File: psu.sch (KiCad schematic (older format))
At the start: 72 parts, among them J10 1053091202, Q10 SQS401EN-T1_BE3, Q5 BSS84PH6327XTSA2, Q6 Si7223DN, Q8 Si7223DN, Q9 Si7223DN, U13 AP62301WU-7, U14 AP62301WU-7, U15 AP62301WU-7, U16 LMV431IM5, U17 AP62301WU-7, U21 LTC4417IUF

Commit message: Change USB-C connectors, continue layout
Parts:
- removed J10: 1053091202, sa800u-baseboard-hw-footprints:1053091202, symbol sa800u-baseboard-hw:1053091202
- added J10: 1053131202, antmicro-footprints:Molex_Nano-Fit_105313-xx02_1x02_P2.50mm_Horizontal, symbol antmicroRectangularConnectorsHeadersFemalePins:1053131202
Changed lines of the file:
@@
-$EndComp
-$Comp
-L sa800u-baseboard-hw:1053091202 J?
-U 1 1 61FFBF6D
-P 675 875
-AR Path="/61A19323/61FFBF6D" Ref="J?"  Part="1"
-AR Path="/61B0DC30/61FFBF6D" Ref="J10"  Part="1"
-F 0 "J10" H 783 1040 50  0000 C CNN
-F 1 "1053091202" H 783 949 50  0000 C CNN
-F 2 "sa800u-baseboard-hw-footprints:1053091202" H 500 550 50  0001 C CNN
-F 3 "" H 675 875 50  0001 C CNN
-F 4 "Molex" H 625 350 50  0001 C CNN "Manufacturer"
-F 5 "1053091202" H 550 425 50  0001 C CNN "MPN"
-	1    675  875
-	1    0    0    -1
 $EndComp
 $Comp
@@
 	0    1    1    0
 $EndComp
-Connection ~ 2500 6150
 $Comp
 L sa800u-baseboard-hw:R_13k7_0402 R140
@@
 	0    1    1    0
 $EndComp
-Connection ~ 2200 7200
-Connection ~ 2800 5100
 Wire Wire Line
 	7150 5000 7150 5250
@@
 Wire Wire Line
 	7150 4700 7150 4600
+$Comp
+L antmicroRectangularConnectorsHeadersFemalePins:1053131202 J10
+U 1 1 620EC9A9
+P 675 875
+F 0 "J10" H 783 1040 50  0000 C CNN
+F 1 "1053131202" H 783 949 50  0000 C CNN
+F 2 "antmicro-footprints:Molex_Nano-Fit_105313-xx02_1x02_P2.50mm_Horizontal" H 500 550 50  0001 C CNN
+F 3 "https://www.molex.com/molex/products/part-detail/pcb_headers/1053131202" H 675 875 50  0001 C CNN
+F 4 "Molex" H 625 350 50  0001 C CNN "Manufacturer"
+F 5 "1053131202" H 550 425 50  0001 C CNN "MPN"
+	1    675  875
+	1    0    0    -1
+$EndComp
 $EndSCHEMATC

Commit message: Change LED to KP-1608EC
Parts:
- J10: symbol antmicroRectangularConnectorsHeadersFemalePins:1053131202 -> sa800u-baseboard-hw-rescue:1053131202-antmicroRectangularConnectorsHeadersFemalePins
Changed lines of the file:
@@
 	7150 4700 7150 4600
 $Comp
-L antmicroRectangularConnectorsHeadersFemalePins:1053131202 J10
+L sa800u-baseboard-hw-rescue:1053131202-antmicroRectangularConnectorsHeadersFemalePins J10
 U 1 1 620EC9A9
 P 675 875
+AR Path="/620EC9A9" Ref="J10"  Part="1"
+AR Path="/61B0DC30/620EC9A9" Ref="J10"  Part="1"
 F 0 "J10" H 783 1040 50  0000 C CNN
 F 1 "1053131202" H 783 949 50  0000 C CNN

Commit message: Add test points
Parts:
- added D?: KP-1608EC, sa800u-baseboard-hw-footprints:LED_0603, symbol sa800u-baseboard-hw:KP-1608EC
- added R?: R_10k_0402, sa800u-baseboard-hw-footprints:0402-res, symbol sa800u-baseboard-hw:R_10k_0402
- added TP? (x24): TP_SMD_0_75MM, antmicro-footprints:Testpoint_smd_0_75mm, symbol antmicroTestPoints:TP_SMD_0_75MM
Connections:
- wire segments 237 -> 247

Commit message: Annotate test points, reimport 510R from global library
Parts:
- gave numbers to parts that had none: 26
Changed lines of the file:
@@
 	7125 1000 7125 950
 $Comp
-L sa800u-baseboard-hw:R_10k_0402 R?
+L sa800u-baseboard-hw:R_10k_0402 R57
 U 1 1 62114A3F
 P 7125 1150
-F 0 "R?" V 7170 1080 60  0000 R CNN
+F 0 "R57" V 7170 1080 60  0000 R CNN
 F 1 "R_10k_0402" H 7125 1000 60  0001 C CNN
 F 2 "sa800u-baseboard-hw-footprints:0402-res" H 7325 1350 60  0001 L CNN
@@
 $EndComp
 $Comp
-L sa800u-baseboard-hw:KP-1608EC D?
+L sa800u-baseboard-hw:KP-1608EC D30
 U 1 1 62114A47
 P 7125 1600
-F 0 "D?" V 6900 1625 60  0000 L CNN
+F 0 "D30" V 6900 1625 60  0000 L CNN
 F 1 "KP-1608EC" H 7075 1831 60  0001 C CNN
 F 2 "sa800u-baseboard-hw-footprints:LED_0603" H 7325 1800 60  0001 L CNN
@@
 P 7125 1700
 AR Path="/6215F5FF" Ref="#PWR?"  Part="1"
-AR Path="/61B0DC30/6215F5FF" Ref="#PWR?"  Part="1"
-F 0 "#PWR?" H 7125 1450 50  0001 C CNN
+AR Path="/61B0DC30/6215F5FF" Ref="#PWR0247"  Part="1"
+F 0 "#PWR0247" H 7125 1450 50  0001 C CNN
 F 1 "GND" H 7130 1527 50  0000 C CNN
 F 2 "" H 7125 1700 50  0001 C CNN
@@
 $EndComp
 $Comp
-L antmicroTestPoints:TP_SMD_0_75MM TP?
+L antmicroTestPoints:TP_SMD_0_75MM TP56
 U 1 1 621521C7
 P 12000 5950
-F 0 "TP?" H 11950 5997 50  0000 R CNN
+F 0 "TP56" H 11950 5997 50  0000 R CNN
 F 1 "TP_SMD_0_75MM" H 12000 5850 50  0001 C CNN
 F 2 "antmicro-footprints:Testpoint_smd_0_75mm" H 12200 6150 60  0001 L CNN
@@
 $EndComp
 $Comp
-L antmicroTestPoints:TP_SMD_0_75MM TP?
+L antmicroTestPoints:TP_SMD_0_75MM TP57
 U 1 1 62156A24
 P 12000 7325
-F 0 "TP?" H 11950 7372 50  0000 R CNN
+F 0 "TP57" H 11950 7372 50  0000 R CNN
 F 1 "TP_SMD_0_75MM" H 12000 7225 50  0001 C CNN
 F 2 "antmicro-footprints:Testpoint_smd_0_75mm" H 12200 7525 60  0001 L CNN
@@
 $EndComp
 $Comp
-L antmicroTestPoints:TP_SMD_0_75MM TP?
+L antmicroTestPoints:TP_SMD_0_75MM TP58
 U 1 1 621677D1
 P 12000 8700
-F 0 "TP?" H 11950 8747 50  0000 R CNN
+F 0 "TP58" H 11950 8747 50  0000 R CNN
 F 1 "TP_SMD_0_75MM" H 12000 8600 50  0001 C CNN
 F 2 "antmicro-footprints:Testpoint_smd_0_75mm" H 12200 8900 60  0001 L CNN
@@
 $EndComp
 $Comp
-L antmicroTestPoints:TP_SMD_0_75MM TP?
+L antmicroTestPoints:TP_SMD_0_75MM TP68
 U 1 1 6217A18F
 P 14625 8700
-F 0 "TP?" H 14575 8747 50  0000 R CNN
+F 0 "TP68" H 14575 8747 50  0000 R CNN
 F 1 "TP_SMD_0_75MM" H 14625 8600 50  0001 C CNN
 F 2 "antmicro-footprints:Testpoint_smd_0_75mm" H 14825 8900 60  0001 L CNN
@@
 $EndComp
 $Comp
-L antmicroTestPoints:TP_SMD_0_75MM TP?
+L antmicroTestPoints:TP_SMD_0_75MM TP67
 U 1 1 6218BBE3
 P 14625 7325
-F 0 "TP?" H 14575 7372 50  0000 R CNN
+F 0 "TP67" H 14575 7372 50  0000 R CNN
 F 1 "TP_SMD_0_75MM" H 14625 7225 50  0001 C CNN
 F 2 "antmicro-footprints:Testpoint_smd_0_75mm" H 14825 7525 60  0001 L CNN
@@
 $EndComp
 $Comp
-L antmicroTestPoints:TP_SMD_0_75MM TP?
+L antmicroTestPoints:TP_SMD_0_75MM TP66
 U 1 1 6219BCD7
 P 14625 5950
-F 0 "TP?" H 14575 5997 50  0000 R CNN
+F 0 "TP66" H 14575 5997 50  0000 R CNN
 F 1 "TP_SMD_0_75MM" H 14625 5850 50  0001 C CNN
 F 2 "antmicro-footprints:Testpoint_smd_0_75mm" H 14825 6150 60  0001 L CNN
@@
 $EndComp
 $Comp
-L antmicroTestPoints:TP_SMD_0_75MM TP?
+L antmicroTestPoints:TP_SMD_0_75MM TP61
 U 1 1 621AD212
 P 12325 6450
-F 0 "TP?" H 12375 6497 50  0000 L CNN
+F 0 "TP61" H 12375 6497 50  0000 L CNN
 F 1 "TP_SMD_0_75MM" H 12325 6350 50  0001 C CNN
 F 2 "antmicro-footprints:Testpoint_smd_0_75mm" H 12525 6650 60  0001 L CNN
@@
 $EndComp
 $Comp
-L antmicroTestPoints:TP_SMD_0_75MM TP?
+L antmicroTestPoints:TP_SMD_0_75MM TP62
 U 1 1 621BF886
 P 12325 7825
-F 0 "TP?" H 12375 7872 50  0000 L CNN
+F 0 "TP62" H 12375 7872 50  0000 L CNN
 F 1 "TP_SMD_0_75MM" H 12325 7725 50  0001 C CNN
 F 2 "antmicro-footprints:Testpoint_smd_0_75mm" H 12525 8025 60  0001 L CNN
@@
 $EndComp
 $Comp
-L antmicroTestPoints:TP_SMD_0_75MM TP?
+L antmicroTestPoints:TP_SMD_0_75MM TP63
 U 1 1 621D2B64
 P 12325 9200
-F 0 "TP?" H 12375 9247 50  0000 L CNN
+F 0 "TP63" H 12375 9247 50  0000 L CNN
 F 1 "TP_SMD_0_75MM" H 12325 9100 50  0001 C CNN
 F 2 "antmicro-footprints:Testpoint_smd_0_75mm" H 12525 9400 60  0001 L CNN
@@
 $EndComp
 $Comp
-L antmicroTestPoints:TP_SMD_0_75MM TP?
+L antmicroTestPoints:TP_SMD_0_75MM TP48
 U 1 1 621EF4D3
 P 5675 4800
-F 0 "TP?" H 5725 4847 50  0000 L CNN
+F 0 "TP48" H 5725 4847 50  0000 L CNN
 F 1 "TP_SMD_0_75MM" H 5675 4700 50  0001 C CNN
 F 2 "antmicro-footprints:Testpoint_smd_0_75mm" H 5875 5000 60  0001 L CNN
@@
 $EndComp
 $Comp
-L antmicroTestPoints:TP_SMD_0_75MM TP?
+L antmicroTestPoints:TP_SMD_0_75MM TP49
 U 1 1 62200067
 P 5975 4800
-F 0 "TP?" H 6025 4847 50  0000 L CNN
+F 0 "TP49" H 6025 4847 50  0000 L CNN
 F 1 "TP_SMD_0_75MM" H 5975 4700 50  0001 C CNN
 F 2 "antmicro-footprints:Testpoint_smd_0_75mm" H 6175 5000 60  0001 L CNN
@@
 $EndComp
 $Comp
-L antmicroTestPoints:TP_SMD_0_75MM TP?
+L antmicroTestPoints:TP_SMD_0_75MM TP51
 U 1 1 6220FE09
 P 6275 4800
-F 0 "TP?" H 6325 4847 50  0000 L CNN
+F 0 "TP51" H 6325 4847 50  0000 L CNN
 F 1 "TP_SMD_0_75MM" H 6275 4700 50  0001 C CNN
 F 2 "antmicro-footprints:Testpoint_smd_0_75mm" H 6475 5000 60  0001 L CNN
@@
 	6275 5250 7150 5250
 $Comp
-L antmicroTestPoints:TP_SMD_0_75MM TP?
+L antmicroTestPoints:TP_SMD_0_75MM TP47
 U 1 1 622544F5
 P 2800 850
-F 0 "TP?" H 2850 897 50  0000 L CNN
+F 0 "TP47" H 2850 897 50  0000 L CNN
 F 1 "TP_SMD_0_75MM" H 2800 750 50  0001 C CNN
 F 2 "antmicro-footprints:Testpoint_smd_0_75mm" H 3000 1050 60  0001 L CNN
@@
 $EndComp
 $Comp
-L antmicroTestPoints:TP_SMD_0_75MM TP?
+L antmicroTestPoints:TP_SMD_0_75MM TP46
 U 1 1 622544FB
 P 2500 1650
-F 0 "TP?" H 2550 1697 50  0000 L CNN
+F 0 "TP46" H 2550 1697 50  0000 L CNN
 F 1 "TP_SMD_0_75MM" H 2500 1550 50  0001 C CNN
 F 2 "antmicro-footprints:Testpoint_smd_0_75mm" H 2700 1850 60  0001 L CNN
@@
 $EndComp
 $Comp
-L antmicroTestPoints:TP_SMD_0_75MM TP?
+L antmicroTestPoints:TP_SMD_0_75MM TP45
 U 1 1 62254501
 P 2200 2500
-F 0 "TP?" H 2250 2547 50  0000 L CNN
+F 0 "TP45" H 2250 2547 50  0000 L CNN
 F 1 "TP_SMD_0_75MM" H 2200 2400 50  0001 C CNN
 F 2 "antmicro-footprints:Testpoint_smd_0_75mm" H 2400 2700 60  0001 L CNN
@@
 	1300 950  2800 950
 $Comp
-L antmicroTestPoints:TP_SMD_0_75MM TP?
+L antmicroTestPoints:TP_SMD_0_75MM TP50
 U 1 1 622BE852
 P 6150 850
-F 0 "TP?" H 6200 897 50  0000 L CNN
+F 0 "TP50" H 6200 897 50  0000 L CNN
 F 1 "TP_SMD_0_75MM" H 6150 750 50  0001 C CNN
 F 2 "antmicro-footprints:Testpoint_smd_0_75mm" H 6350 1050 60  0001 L CNN
@@
 $EndComp
 $Comp
-L antmicroTestPoints:TP_SMD_0_75MM TP?
+L antmicroTestPoints:TP_SMD_0_75MM TP55
 U 1 1 622DD73E
 P 11675 1900
-F 0 "TP?" H 11725 1947 50  0000 L CNN
+F 0 "TP55" H 11725 1947 50  0000 L CNN
 F 1 "TP_SMD_0_75MM" H 11675 1800 50  0001 C CNN
 F 2 "antmicro-footprints:Testpoint_smd_0_75mm" H 11875 2100 60  0001 L CNN
@@
 $EndComp
 $Comp
-L antmicroTestPoints:TP_SMD_0_75MM TP?
+L antmicroTestPoints:TP_SMD_0_75MM TP60
 U 1 1 622EFCB5
 P 12225 3000
-F 0 "TP?" H 12275 3047 50  0000 L CNN
+F 0 "TP60" H 12275 3047 50  0000 L CNN
 F 1 "TP_SMD_0_75MM" H 12225 2900 50  0001 C CNN
 F 2 "antmicro-footprints:Testpoint_smd_0_75mm" H 12425 3200 60  0001 L CNN
@@
 $EndComp
 $Comp
-L antmicroTestPoints:TP_SMD_0_75MM TP?
+L antmicroTestPoints:TP_SMD_0_75MM TP65
 U 1 1 62302665
 P 14550 2500
-F 0 "TP?" H 14600 2547 50  0000 L CNN
+F 0 "TP65" H 14600 2547 50  0000 L CNN
 F 1 "TP_SMD_0_75MM" H 14550 2400 50  0001 C CNN
 F 2 "antmicro-footprints:Testpoint_smd_0_75mm" H 14750 2700 60  0001 L CNN
@@
 $EndComp
 $Comp
-L antmicroTestPoints:TP_SMD_0_75MM TP?
+L antmicroTestPoints:TP_SMD_0_75MM TP59
 U 1 1 62313708
 P 12225 2500
-F 0 "TP?" H 12275 2547 50  0000 L CNN
+F 0 "TP59" H 12275 2547 50  0000 L CNN
 F 1 "TP_SMD_0_75MM" H 12225 2400 50  0001 C CNN
 F 2 "antmicro-footprints:Testpoint_smd_0_75mm" H 12425 2700 60  0001 L CNN
@@
 $EndComp
 $Comp
-L antmicroTestPoints:TP_SMD_0_75MM TP?
+L antmicroTestPoints:TP_SMD_0_75MM TP52
 U 1 1 6232A519
 P 9725 2575
-F 0 "TP?" V 9825 2500 50  0000 C CNN
+F 0 "TP52" V 9825 2500 50  0000 C CNN
 F 1 "TP_SMD_0_75MM" H 9725 2475 50  0001 C CNN
 F 2 "antmicro-footprints:Testpoint_smd_0_75mm" H 9925 2775 60  0001 L CNN
@@
 $EndComp
 $Comp
-L antmicroTestPoints:TP_SMD_0_75MM TP?
+L antmicroTestPoints:TP_SMD_0_75MM TP53
 U 1 1 62350CD4
 P 9825 1425
-F 0 "TP?" H 9875 1472 50  0000 L CNN
+F 0 "TP53" H 9875 1472 50  0000 L CNN
 F 1 "TP_SMD_0_75MM" H 9825 1325 50  0001 C CNN
 F 2 "antmicro-footprints:Testpoint_smd_0_75mm" H 10025 1625 60  0001 L CNN
@@
 $EndComp
 $Comp
-L antmicroTestPoints:TP_SMD_0_75MM TP?
+L antmicroTestPoints:TP_SMD_0_75MM TP54
 U 1 1 62365069
 P 10125 2025
-F 0 "TP?" V 10125 1976 50  0000 R CNN
+F 0 "TP54" V 10125 1976 50  0000 R CNN
 F 1 "TP_SMD_0_75MM" H 10125 1925 50  0001 C CNN
 F 2 "antmicro-footprints:Testpoint_smd_0_75mm" H 10325 2225 60  0001 L CNN
@@
 $EndComp
 $Comp
-L antmicroTestPoints:TP_SMD_0_75MM TP?
+L antmicroTestPoints:TP_SMD_0_75MM TP64
 U 1 1 623815DB
 P 14525 1425
-F 0 "TP?" H 14575 1472 50  0000 L CNN
+F 0 "TP64" H 14575 1472 50  0000 L CNN
 F 1 "TP_SMD_0_75MM" H 14525 1325 50  0001 C CNN
 F 2 "antmicro-footprints:Testpoint_smd_0_75mm" H 14725 1625 60  0001 L CNN

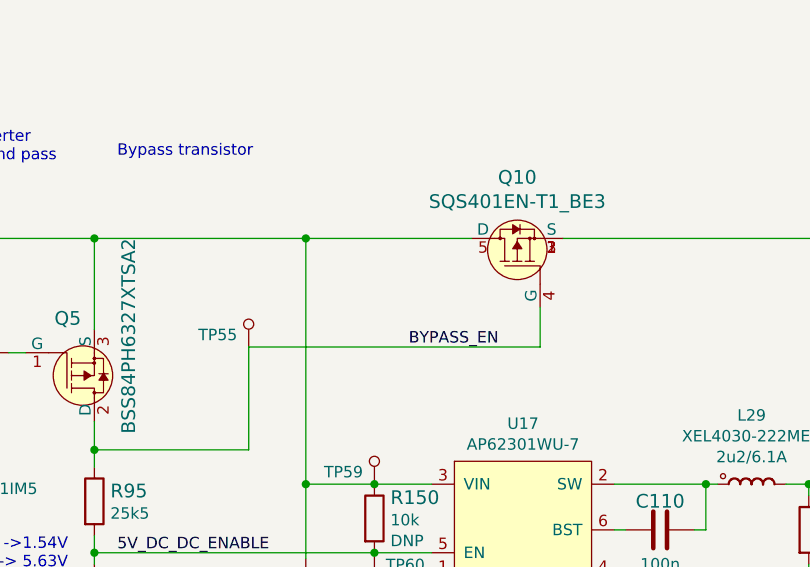
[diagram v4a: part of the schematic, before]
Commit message: Fix labels, fix p-mosfet symbol
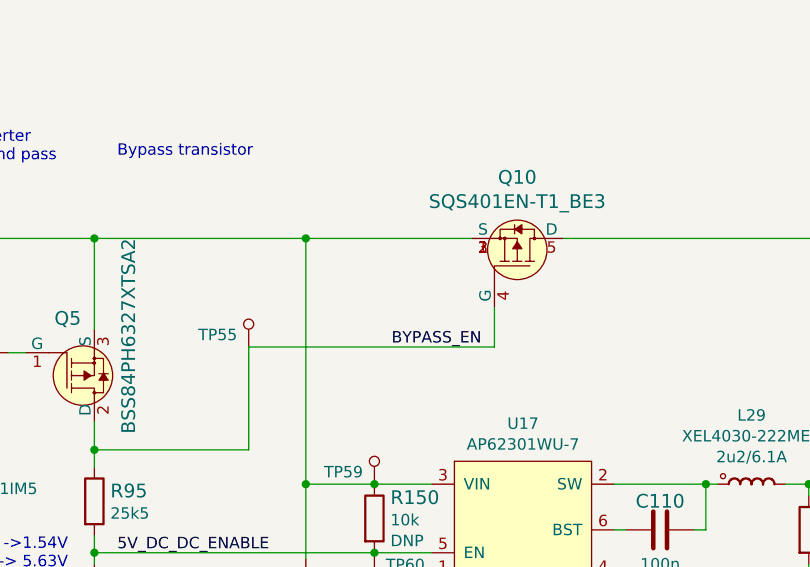
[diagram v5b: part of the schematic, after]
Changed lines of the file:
@@
 F 5 "Vishay" H 13050 2625 60  0001 L CNN "Manufacturer"
 	1    12850 1525
-	0    -1   -1   0
+	0    1    -1   0
 $EndComp
 Text Notes 11100 1175 0    50   ~ 0
@@
 	13050 1525 14525 1525
 Wire Wire Line
-	12950 1825 12950 2000
-Wire Wire Line
-	12950 2000 11675 2000
-Wire Wire Line
 	11925 2600 11925 1525
 Wire Wire Line
@@
 Text Notes 8375 1375 0    79   ~ 16
 5V\n\n
-Text Label 12375 2000 0    50   ~ 0
+Text Label 12300 2000 0    50   ~ 0
 BYPASS_EN
 $Comp
@@
 Wire Wire Line
 	14525 1525 15300 1525
+Wire Wire Line
+	12750 1825 12750 2000
+Wire Wire Line
+	12750 2000 11675 2000
 $EndSCHEMATC

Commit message: Loclib
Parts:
- J10: footprint antmicro-footprints:Molex_Nano-Fit_105313-xx02_1x02_P2.50mm_Horizontal -> sa800u-baseboard-hw-footprints:Molex_Nano-Fit_105313-xx02_1x02_P2.50mm_Horizontal; symbol sa800u-baseboard-hw-rescue:1053131202-antmicroRectangularConnectorsHeadersFemalePins -> sa800u-baseboard-hw:1053131202-antmicroRectangularConnectorsHeadersFemalePins
- TP45, TP46, TP47, TP48, TP49, TP50, TP51, TP52, TP53, TP54, TP55, TP56, TP57, TP58, TP59, TP60, TP61, TP62, TP63, TP64, TP65, TP66, TP67, TP68: footprint antmicro-footprints:Testpoint_smd_0_75mm -> sa800u-baseboard-hw-footprints:Testpoint_smd_0_75mm; symbol antmicroTestPoints:TP_SMD_0_75MM -> sa800u-baseboard-hw:TP_SMD_0_75MM

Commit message: Fix J9 symbol
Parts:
- removed J10: 1053131202, sa800u-baseboard-hw-footprints:Molex_Nano-Fit_105313-xx02_1x02_P2.50mm_Horizontal, symbol sa800u-baseboard-hw:1053131202-antmicroRectangularConnectorsHeadersFemalePins
- added J9: 1053131202, antmicro-footprints:Molex_Nano-Fit_105313-xx02_1x02_P2.50mm_Horizontal, symbol antmicroRectangularConnectorsHeadersFemalePins:1053131202
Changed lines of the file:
@@
 Text GLabel 11175 9100 0    50   Input ~ 0
 1V2_SYS_EN
-$Comp
-L sa800u-baseboard-hw:R_13k7_0402 R143
-U 1 1 62A76BE5
-P 2500 6300
-F 0 "R143" V 2455 6370 60  0000 L CNN
-F 1 "R_13k7_0402" H 2500 6150 60  0001 C CNN
-F 2 "sa800u-baseboard-hw-footprints:0402-res" H 2700 6500 60  0001 L CNN
-F 3 "" H 2500 6300 50  0001 C CNN
-F 4 "Bourns" H 2700 6700 60  0001 L CNN "Manufacturer"
-F 5 "CR0402-FX-1372GLF" H 2700 6600 60  0001 L CNN "MPN"
-F 6 "13k7" V 2553 6370 50  0000 L CNN "Val"
-	1    2500 6300
-	0    1    1    0
-$EndComp
-$Comp
-L sa800u-baseboard-hw:R_13k7_0402 R140
-U 1 1 62A794E7
-P 2200 7350
-F 0 "R140" V 2155 7420 60  0000 L CNN
-F 1 "R_13k7_0402" H 2200 7200 60  0001 C CNN
-F 2 "sa800u-baseboard-hw-footprints:0402-res" H 2400 7550 60  0001 L CNN
-F 3 "" H 2200 7350 50  0001 C CNN
-F 4 "Bourns" H 2400 7750 60  0001 L CNN "Manufacturer"
-F 5 "CR0402-FX-1372GLF" H 2400 7650 60  0001 L CNN "MPN"
-F 6 "13k7" V 2253 7420 50  0000 L CNN "Val"
-	1    2200 7350
-	0    1    1    0
-$EndComp
-$Comp
-L sa800u-baseboard-hw:R_13k7_0402 R158
-U 1 1 62A8AC23
-P 2800 5250
-F 0 "R158" V 2755 5320 60  0000 L CNN
-F 1 "R_13k7_0402" H 2800 5100 60  0001 C CNN
-F 2 "sa800u-baseboard-hw-footprints:0402-res" H 3000 5450 60  0001 L CNN
-F 3 "" H 2800 5250 50  0001 C CNN
-F 4 "Bourns" H 3000 5650 60  0001 L CNN "Manufacturer"
-F 5 "CR0402-FX-1372GLF" H 3000 5550 60  0001 L CNN "MPN"
-F 6 "13k7" V 2853 5320 50  0000 L CNN "Val"
-	1    2800 5250
-	0    1    1    0
-$EndComp
 Wire Wire Line
 	7150 5000 7150 5250
@@
 Wire Wire Line
 	7150 4700 7150 4600
-$Comp
-L sa800u-baseboard-hw:1053131202-antmicroRectangularConnectorsHeadersFemalePins J10
-U 1 1 620EC9A9
-P 675 875
-AR Path="/620EC9A9" Ref="J10"  Part="1"
-AR Path="/61B0DC30/620EC9A9" Ref="J10"  Part="1"
-F 0 "J10" H 783 1040 50  0000 C CNN
-F 1 "1053131202" H 783 949 50  0000 C CNN
-F 2 "sa800u-baseboard-hw-footprints:Molex_Nano-Fit_105313-xx02_1x02_P2.50mm_Horizontal" H 500 550 50  0001 C CNN
-F 3 "https://www.molex.com/molex/products/part-detail/pcb_headers/1053131202" H 675 875 50  0001 C CNN
-F 4 "Molex" H 625 350 50  0001 C CNN "Manufacturer"
-F 5 "1053131202" H 550 425 50  0001 C CNN "MPN"
-	1    675  875
-	1    0    0    -1
-$EndComp
 Wire Wire Line
 	7125 1000 7125 950
@@
 Wire Wire Line
 	12750 2000 11675 2000
+$Comp
+L antmicroRectangularConnectorsHeadersFemalePins:1053131202 J9
+U 1 1 62850090
+P 675 875
+F 0 "J9" H 783 1040 50  0000 C CNN
+F 1 "1053131202" H 783 949 50  0000 C CNN
+F 2 "antmicro-footprints:Molex_Nano-Fit_105313-xx02_1x02_P2.50mm_Horizontal" H 500 550 50  0001 C CNN
+F 3 "https://www.molex.com/molex/products/part-detail/pcb_headers/1053131202" H 675 875 50  0001 C CNN
+F 4 "Molex" H 625 350 50  0001 C CNN "Manufacturer"
+F 5 "1053131202" H 550 425 50  0001 C CNN "MPN"
+	1    675  875
+	1    0    0    -1
+$EndComp
+$Comp
+L sa800u-baseboard-hw:R_13k7_0402 R140
+U 1 1 62A794E7
+P 2200 7350
+F 0 "R140" V 2155 7420 60  0000 L CNN
+F 1 "R_13k7_0402" H 2200 7200 60  0001 C CNN
+F 2 "sa800u-baseboard-hw-footprints:0402-res" H 2400 7550 60  0001 L CNN
+F 3 "" H 2200 7350 50  0001 C CNN
+F 4 "Bourns" H 2400 7750 60  0001 L CNN "Manufacturer"
+F 5 "CR0402-FX-1372GLF" H 2400 7650 60  0001 L CNN "MPN"
+F 6 "13k7" V 2253 7420 50  0000 L CNN "Val"
+	1    2200 7350
+	0    1    1    0
+$EndComp
+$Comp
+L sa800u-baseboard-hw:R_13k7_0402 R143
+U 1 1 62A76BE5
+P 2500 6300
+F 0 "R143" V 2455 6370 60  0000 L CNN
+F 1 "R_13k7_0402" H 2500 6150 60  0001 C CNN
+F 2 "sa800u-baseboard-hw-footprints:0402-res" H 2700 6500 60  0001 L CNN
+F 3 "" H 2500 6300 50  0001 C CNN
+F 4 "Bourns" H 2700 6700 60  0001 L CNN "Manufacturer"
+F 5 "CR0402-FX-1372GLF" H 2700 6600 60  0001 L CNN "MPN"
+F 6 "13k7" V 2553 6370 50  0000 L CNN "Val"
+	1    2500 6300
+	0    1    1    0
+$EndComp
+$Comp
+L sa800u-baseboard-hw:R_13k7_0402 R158
+U 1 1 62A8AC23
+P 2800 5250
+F 0 "R158" V 2755 5320 60  0000 L CNN
+F 1 "R_13k7_0402" H 2800 5100 60  0001 C CNN
+F 2 "sa800u-baseboard-hw-footprints:0402-res" H 3000 5450 60  0001 L CNN
+F 3 "" H 2800 5250 50  0001 C CNN
+F 4 "Bourns" H 3000 5650 60  0001 L CNN "Manufacturer"
+F 5 "CR0402-FX-1372GLF" H 3000 5550 60  0001 L CNN "MPN"
+F 6 "13k7" V 2853 5320 50  0000 L CNN "Val"
+	1    2800 5250
+	0    1    1    0
+$EndComp
 $EndSCHEMATC

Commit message: Loclib
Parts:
- J9: footprint antmicro-footprints:Molex_Nano-Fit_105313-xx02_1x02_P2.50mm_Horizontal -> sa800u-baseboard-hw-footprints:Molex_Nano-Fit_105313-xx02_1x02_P2.50mm_Horizontal; symbol antmicroRectangularConnectorsHeadersFemalePins:1053131202 -> sa800u-baseboard-hw:1053131202
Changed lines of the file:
@@
 	12750 2000 11675 2000
 $Comp
-L antmicroRectangularConnectorsHeadersFemalePins:1053131202 J9
+L sa800u-baseboard-hw:1053131202 J9
 U 1 1 62850090
 P 675 875
 F 0 "J9" H 783 1040 50  0000 C CNN
 F 1 "1053131202" H 783 949 50  0000 C CNN
-F 2 "antmicro-footprints:Molex_Nano-Fit_105313-xx02_1x02_P2.50mm_Horizontal" H 500 550 50  0001 C CNN
+F 2 "sa800u-baseboard-hw-footprints:Molex_Nano-Fit_105313-xx02_1x02_P2.50mm_Horizontal" H 500 550 50  0001 C CNN
 F 3 "https://www.molex.com/molex/products/part-detail/pcb_headers/1053131202" H 675 875 50  0001 C CNN
 F 4 "Molex" H 625 350 50  0001 C CNN "Manufacturer"
